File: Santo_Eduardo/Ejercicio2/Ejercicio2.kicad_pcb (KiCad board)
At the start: 2 copper layers, 40.6 x 61 mm, 13 parts, among them J1 DB9, U1 AMIS42665TJAA1RG, U2 MAX232

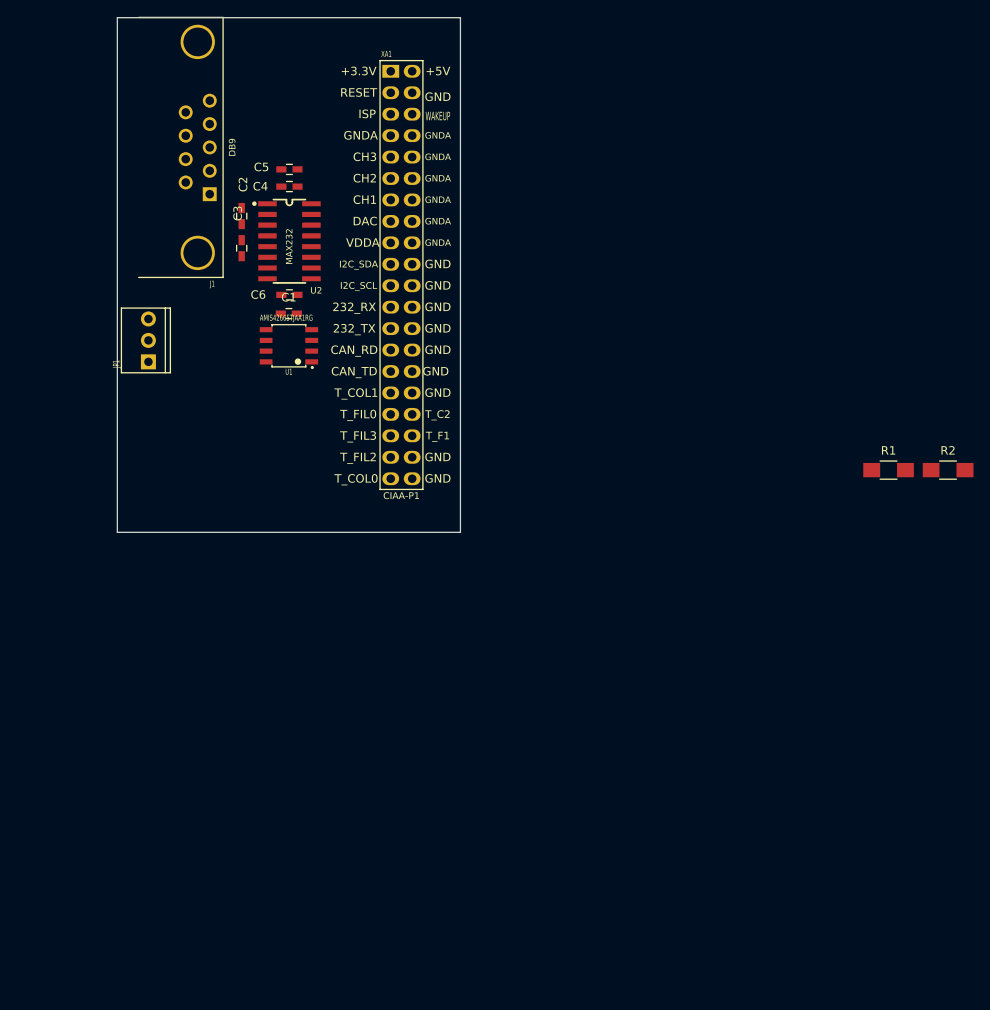
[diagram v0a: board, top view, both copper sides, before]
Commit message: Cambiados footprints Revisando placement en PCB
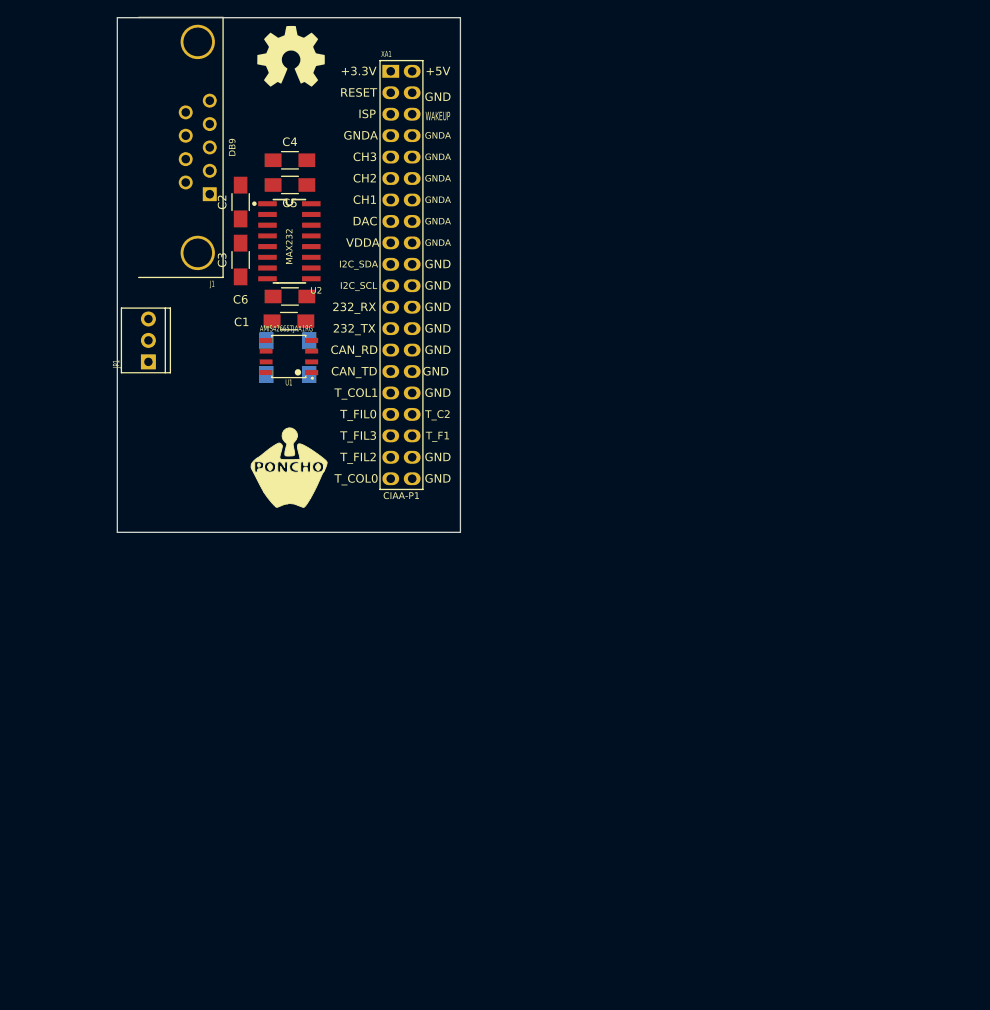
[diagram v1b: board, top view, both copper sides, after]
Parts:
- added G***: LOGO, Ejercicio2:Logo_Poncho, F.Cu at (158.8, 74.3)
- added G101: Logo_OSHWA, Ejercicio2:Logo_OSHWA, F.Cu at (159.0, 25.5)
- C1, C2, C3, C4, C5, C6: footprint Ejercicio2:C_0603_HandSoldering -> Ejercicio2:1206
- R1, R2: moved to B.Cu
- moved R2 76.8 mm to (161.2, 61.2), turned to 270 degrees
- moved R1 74.9 mm to (156.1, 61.2), turned to 90 degrees
- moved C2 1.66 mm to (153.0, 42.8)
- moved C3 1.40 mm to (153.0, 49.7)
- moved U1 1.27 mm to (158.8, 61.1)
- moved C4 1.08 mm to (158.9, 37.8)
- moved C1 0.89 mm to (158.8, 56.9)
- moved C5 0.20 mm to (158.9, 40.8)
- moved C6 0.20 mm to (158.9, 54.0)
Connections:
- J1 pad 1: Net-(J1-Pad1) -> (no net)
- J1 pad 4: Net-(J1-Pad4) -> (no net)
- J1 pad 6: Net-(J1-Pad6) -> (no net)
- J1 pad 9: Net-(J1-Pad9) -> (no net)
- XA1 pad 10: Net-(XA1-Pad10) -> (no net)
- XA1 pad 11: Net-(XA1-Pad11) -> (no net)
- XA1 pad 12: Net-(XA1-Pad12) -> (no net)
- XA1 pad 13: Net-(XA1-Pad13) -> (no net)
- XA1 pad 14: Net-(XA1-Pad14) -> (no net)
- XA1 pad 15: Net-(XA1-Pad15) -> (no net)
- XA1 pad 16: Net-(XA1-Pad16) -> (no net)
- XA1 pad 17: Net-(XA1-Pad17) -> (no net)
- XA1 pad 18: Net-(XA1-Pad18) -> (no net)
- XA1 pad 19: Net-(XA1-Pad19) -> (no net)
- XA1 pad 21: Net-(XA1-Pad21) -> (no net)
- XA1 pad 3: Net-(XA1-Pad3) -> (no net)
- XA1 pad 31: Net-(XA1-Pad31) -> (no net)
- XA1 pad 33: Net-(XA1-Pad33) -> (no net)
- XA1 pad 34: Net-(XA1-Pad34) -> (no net)
- XA1 pad 36: Net-(XA1-Pad36) -> (no net)
- XA1 pad 39: Net-(XA1-Pad39) -> (no net)
- XA1 pad 5: Net-(XA1-Pad5) -> (no net)
- XA1 pad 6: Net-(XA1-Pad6) -> (no net)
- XA1 pad 7: Net-(XA1-Pad7) -> (no net)
- XA1 pad 8: Net-(XA1-Pad8) -> (no net)
- XA1 pad 9: Net-(XA1-Pad9) -> (no net)

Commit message: Minor changes on pcb
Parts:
- moved R2 4.95 mm to (156.2, 61.1)
- moved R1 4.07 mm to (152.0, 61.1)
- moved C2 2.82 mm to (152.7, 40.0)
- moved C3 2.57 mm to (152.7, 47.1)
- moved G101 1.66 mm to (158.9, 27.2)
- moved JP1 0.52 mm to (141.6, 59.1)
- moved G*** 0.52 mm to (158.9, 73.8)
- moved C1 0.40 mm to (158.9, 56.5)
- moved U1 0.18 mm to (158.9, 61.0)
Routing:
- net GND: track 0.00 -> 147.7 mm, vias 0 -> 4
- net +5V: track 0.00 -> 50.3 mm, vias 0 -> 1
- net Net-(J1-Pad7): track 0.00 -> 32.9 mm, vias 0 -> 1
- net Net-(J1-Pad8): track 0.00 -> 31.6 mm
- net /Conector y CAN/RTS: track 0.00 -> 27.5 mm, vias 0 -> 1
- net +3.3V: track 0.00 -> 26.9 mm
- net /Conector y CAN/CTS: track 0.00 -> 26.0 mm, vias 0 -> 1
- net Net-(J1-Pad3): track 0.00 -> 25.9 mm, vias 0 -> 1
- net Net-(J1-Pad2): track 0.00 -> 20.0 mm, vias 0 -> 1
- net /Conector y CAN/CAN_L: track 0.00 -> 18.9 mm, vias 0 -> 1
- net /Conector y CAN/CAN_H: track 0.00 -> 17.8 mm, vias 0 -> 1
- net /Conector y CAN/RXD: track 0.00 -> 14.9 mm
- net /Conector y CAN/TXD: track 0.00 -> 13.6 mm
- net /Conector y CAN/CANRX: track 0.00 -> 9.76 mm
- net /Conector y CAN/CANTX: track 0.00 -> 9.24 mm
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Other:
- net class Default: clearance 0.2 -> 0.3048; trace_width 0.25 -> 0.3048
- rule trace_clearance: 0.2 -> 0.3048

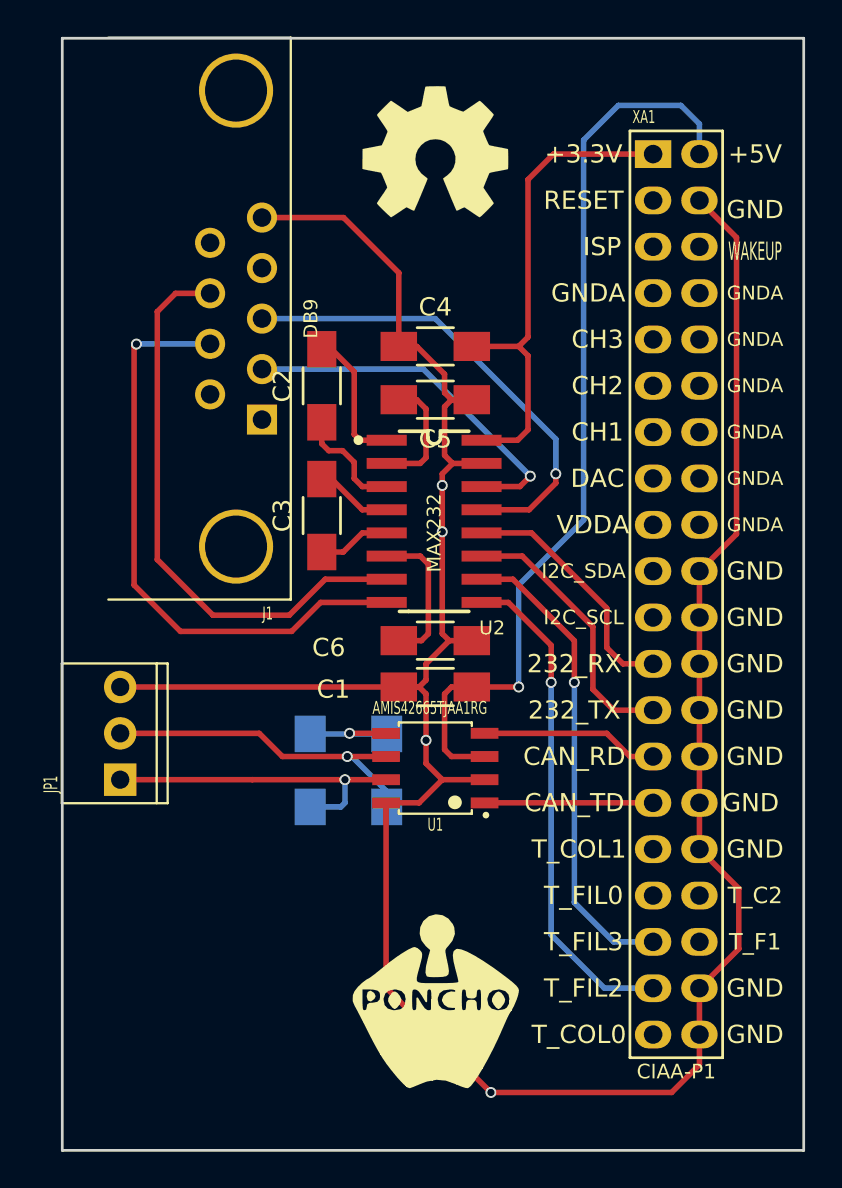
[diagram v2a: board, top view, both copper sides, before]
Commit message: Added GND planes
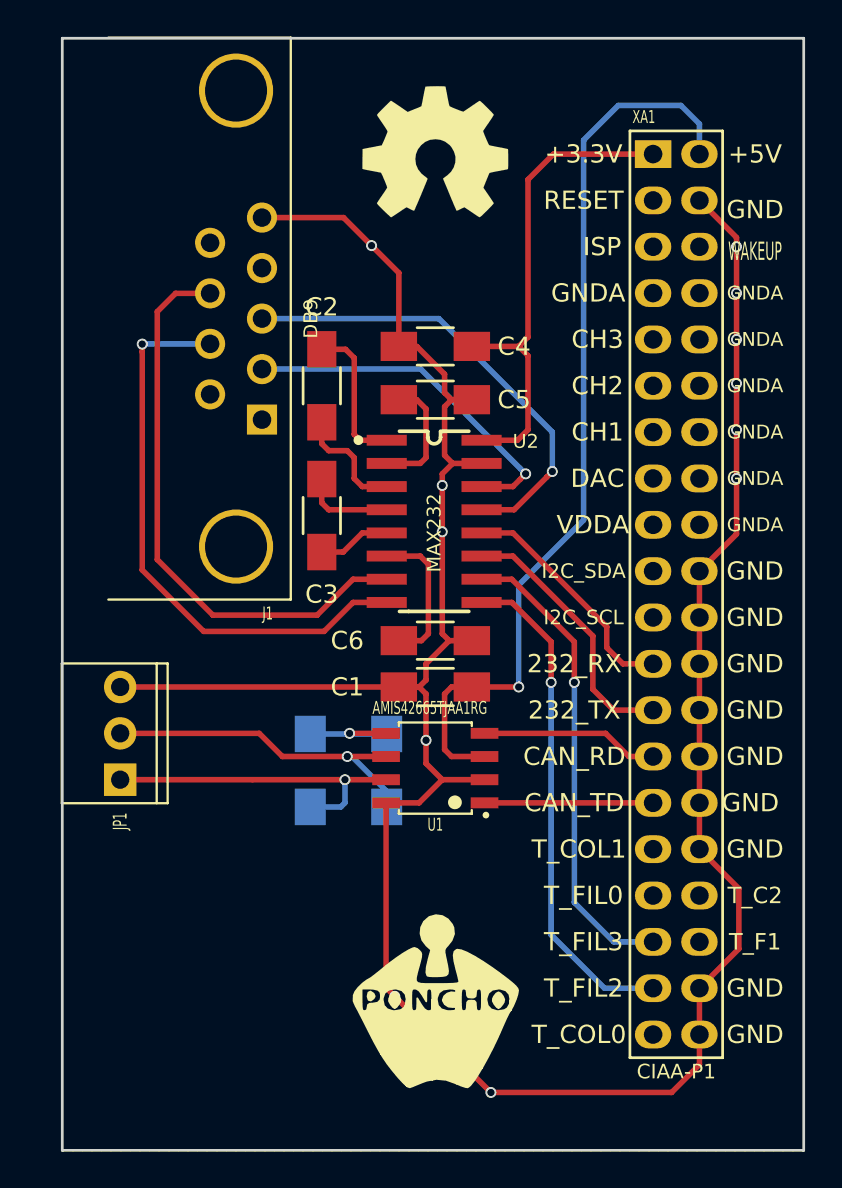
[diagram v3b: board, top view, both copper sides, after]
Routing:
- net Net-(J1-Pad7): track 32.9 -> 31.6 mm
- net Net-(C3-Pad1): track 4.26 -> 5.02 mm
- net /Conector y CAN/TXD: track 13.6 -> 13.0 mm
- net Net-(J1-Pad3): track 25.9 -> 25.4 mm
- net Net-(J1-Pad2): track 20.0 -> 19.5 mm
- net GND: vias 4 -> 13
- added copper zone on B.Cu, net GND
- added copper zone on F.Cu, net GND

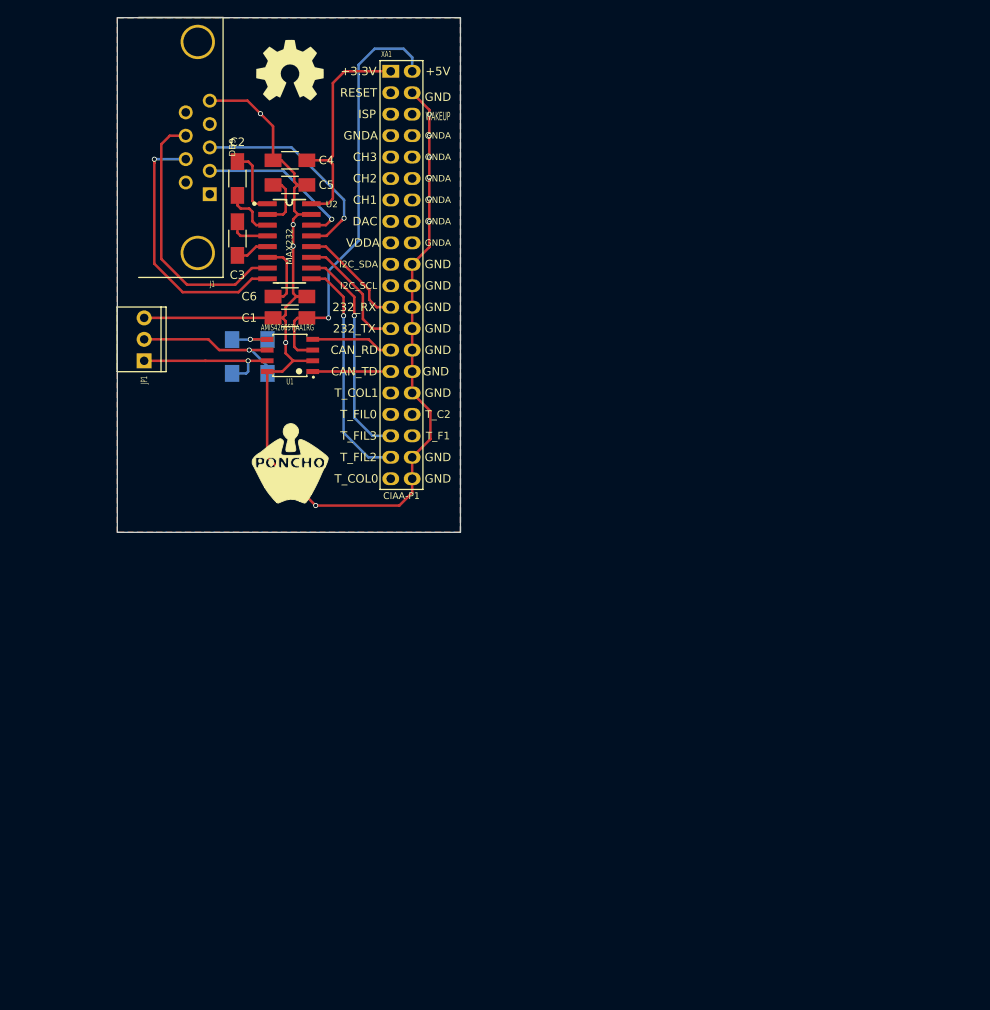
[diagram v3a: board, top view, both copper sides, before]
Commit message: agregadas leyendas, cutouts y keepouts
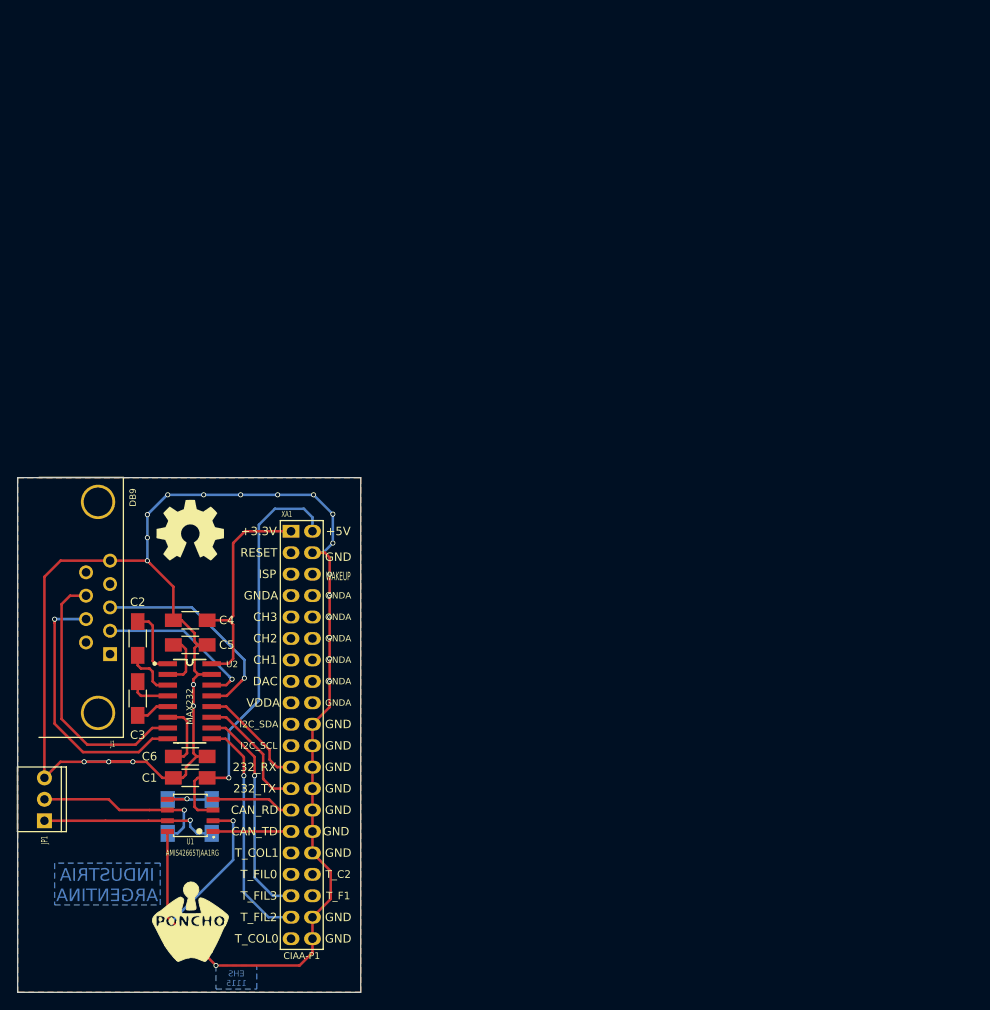
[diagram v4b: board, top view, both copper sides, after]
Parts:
- moved C1 55.7 mm to (147.1, 111.0)
- moved G101 55.7 mm to (147.1, 81.7)
- moved J1 55.7 mm to (136.1, 90.8)
- moved U2 55.7 mm to (147.0, 101.9)
- moved C2 55.7 mm to (140.8, 94.5)
- moved C3 55.7 mm to (140.8, 101.6)
- moved C4 55.7 mm to (147.1, 92.3)
- moved C5 55.7 mm to (147.1, 95.2)
- moved C6 55.7 mm to (147.1, 108.5)
- moved JP1 55.7 mm to (129.8, 113.5)
- moved U1 55.7 mm to (147.1, 115.4)
- moved XA1 55.7 mm to (159.0, 81.8)
- moved R2 55.7 mm to (144.4, 115.6)
- moved G*** 55.6 mm to (147.1, 128.1)
- moved R1 54.5 mm to (149.6, 115.6)
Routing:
- net GND: track 147.7 -> 229.8 mm, vias 13 -> 25
- net /Conector y CAN/CAN_L: track 18.9 -> 22.2 mm
- net /Conector y CAN/CAN_H: track 17.8 -> 20.9 mm
- net Net-(R1-Pad2): track 6.22 -> 7.72 mm
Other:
- board text added: "EHS 1115"
- board text added: "INDUSTRIA ARGENTINA"

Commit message: Added 3D
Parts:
- renumbered G*** to G102
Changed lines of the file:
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@@
     (links 44)
     (no_connects 0)
-    (area 120.475699 75.036699 167.334001 137.0941)
+    (area 126.543999 75.362999 167.334001 136.473001)
     (thickness 1.6)
     (drawings 6)
@@
     (pad 10 thru_hole circle (at -12.4968 0 90) (size 4.064 4.064) (drill 3.4) (layers *.Cu *.Mask))
     (pad 11 thru_hole circle (at 12.4968 0 90) (size 4.064 4.064) (drill 3.4) (layers *.Cu *.Mask))
-    (model ${KIPRJMOD}/ej2.3dshapes/db_9f.wrl
-      (at (xyz 0 0.31 0))
-      (scale (xyz 1 1.1 1))
+    (model ${KIPRJMOD}/Ejercicio2.3dshapes/db_9f.wrl
+      (at (xyz 0 0.28 0))
+      (scale (xyz 1 1 1))
       (rotate (xyz 0 0 180))
     )
@@
     (pad 3 thru_hole circle (at 2.54 0 90) (size 1.778 1.778) (drill 1) (layers *.Cu *.Mask)
       (net 1 GND))
-    (model ${KIPRJMOD}/ej2.3dshapes/CON_PALETA_3.wrl
+    (model ${KIPRJMOD}/Ejercicio2.3dshapes/CON_PALETA_3.wrl
       (at (xyz 0 0.012 0))
       (scale (xyz 0.395 0.395 0.395))
@@
     (pad 2 smd rect (at 2 0 90) (size 2 1.7) (layers B.Cu B.Paste B.Mask)
       (net 16 "Net-(R1-Pad2)"))
-    (model Resistors_SMD.3dshapes/R_1206_HandSoldering.wrl
+    (model ${KIPRJMOD}/Ejercicio2.3dshapes/R_1206_HandSoldering.wrl
       (at (xyz 0 0 0))
       (scale (xyz 1 1 1))
@@
     (pad 2 smd rect (at 2 0 270) (size 2 1.7) (layers B.Cu B.Paste B.Mask)
       (net 15 "/Conector y CAN/CAN_L"))
-    (model Resistors_SMD.3dshapes/R_1206_HandSoldering.wrl
+    (model ${KIPRJMOD}/Ejercicio2.3dshapes/R_1206_HandSoldering.wrl
       (at (xyz 0 0 0))
       (scale (xyz 1 1 1))
@@
     (pad 8 smd rect (at 2.7 -1.905 90) (size 0.6 1.52) (layers F.Cu F.Paste F.Mask)
       (net 1 GND))
-    (model ${KIPRJMOD}/ej2.3dshapes/so-8.wrl
+    (model ${KIPRJMOD}/Ejercicio2.3dshapes/so-8.wrl
       (at (xyz 0 0 0))
       (scale (xyz 1 1 1))
@@
     (pad 16 smd rect (at -4.445 -2.59842 270) (size 0.59944 2.19964) (layers F.Cu F.Paste F.Mask)
       (net 7 +3.3V))
-    (model ${KIPRJMOD}/ej2.3dshapes/so-16.wrl
+    (model ${KIPRJMOD}/Ejercicio2.3dshapes/so-16.wrl
       (at (xyz 0 0 0))
       (scale (xyz 1 1 1))
@@
     (pad 30 thru_hole oval (at 2.54 35.56 270) (size 1.524 2) (drill 1.016) (layers *.Cu *.Mask)
       (net 1 GND))
-    (model ${KIPRJMOD}/ej2.3dshapes/pin_strip_20x2.wrl
+    (model ${KIPRJMOD}/Ejercicio2.3dshapes/pin_strip_20x2.wrl
       (at (xyz 0.05 -0.95 -0.063))
       (scale (xyz 1 1 1))
@@
     (pad 2 smd rect (at 2 0) (size 2 1.6) (layers F.Cu F.Paste F.Mask)
       (net 2 +5V))
+    (model ${KIPRJMOD}/Ejercicio2.3dshapes/C_1206_HandSoldering.wrl
+      (at (xyz 0 0 0))
+      (scale (xyz 1 1 1))
+      (rotate (xyz 0 0 0))
+    )
   )
   (module Ejercicio2:1206 (layer F.Cu)
@@
     (pad 2 smd rect (at 2 0 270) (size 2 1.6) (layers F.Cu F.Paste F.Mask)
       (net 4 "Net-(C2-Pad2)"))
+    (model ${KIPRJMOD}/Ejercicio2.3dshapes/C_1206_HandSoldering.wrl
+      (at (xyz 0 0 0))
+      (scale (xyz 1 1 1))
+      (rotate (xyz 0 0 0))
+    )
   )
   (module Ejercicio2:1206 (layer F.Cu)
@@
     (pad 2 smd rect (at 2 0 270) (size 2 1.6) (layers F.Cu F.Paste F.Mask)
       (net 6 "Net-(C3-Pad2)"))
+    (model ${KIPRJMOD}/Ejercicio2.3dshapes/C_1206_HandSoldering.wrl
+      (at (xyz 0 0 0))
+      (scale (xyz 1 1 1))
+      (rotate (xyz 0 0 0))
+    )
   )
   (module Ejercicio2:1206 (layer F.Cu)
@@
     (pad 2 smd rect (at 2 0 180) (size 2 1.6) (layers F.Cu F.Paste F.Mask)
       (net 1 GND))
+    (model ${KIPRJMOD}/Ejercicio2.3dshapes/C_1206_HandSoldering.wrl
+      (at (xyz 0 0 0))
+      (scale (xyz 1 1 1))
+      (rotate (xyz 0 0 0))
+    )
   )
   (module Ejercicio2:1206 (layer F.Cu)
@@
     (pad 2 smd rect (at 2 0) (size 2 1.6) (layers F.Cu F.Paste F.Mask)
       (net 1 GND))
+    (model ${KIPRJMOD}/Ejercicio2.3dshapes/C_1206_HandSoldering.wrl
+      (at (xyz 0 0 0))
+      (scale (xyz 1 1 1))
+      (rotate (xyz 0 0 0))
+    )
   )
   (module Ejercicio2:1206 (layer F.Cu)
@@
     (pad 2 smd rect (at 2 0) (size 2 1.6) (layers F.Cu F.Paste F.Mask)
       (net 1 GND))
+    (model ${KIPRJMOD}/Ejercicio2.3dshapes/C_1206_HandSoldering.wrl
+      (at (xyz 0 0 0))
+      (scale (xyz 1 1 1))
+      (rotate (xyz 0 0 0))
+    )
   )
   (module Ejercicio2:Logo_Poncho (layer F.Cu)
     (at 147.066 128.0795)
-    (fp_text reference G*** (at 0.127 5.588) (layer F.SilkS) hide
+    (fp_text reference G102 (at 0.127 5.588) (layer F.SilkS) hide
       (effects (font (thickness 0.3)))
     )
